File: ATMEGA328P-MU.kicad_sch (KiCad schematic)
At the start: 14 parts, among them J3 M20-9980345, U4 ATMEGA328P-MU, Y1 CSTNE16M0V530000R0

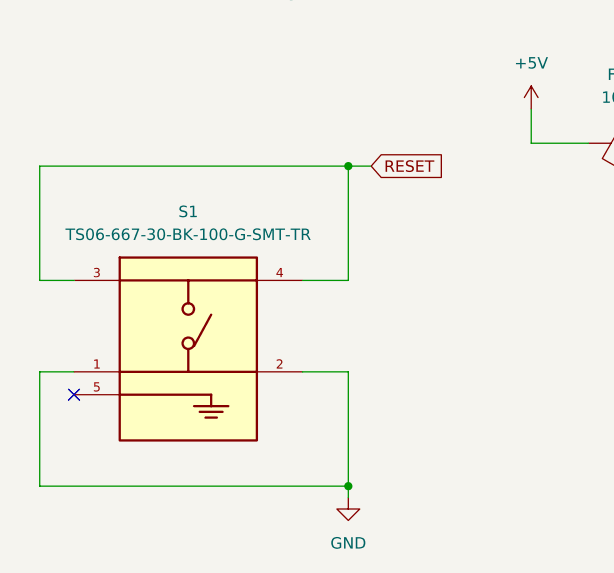
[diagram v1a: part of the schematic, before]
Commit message: Update Multiduino v2 design
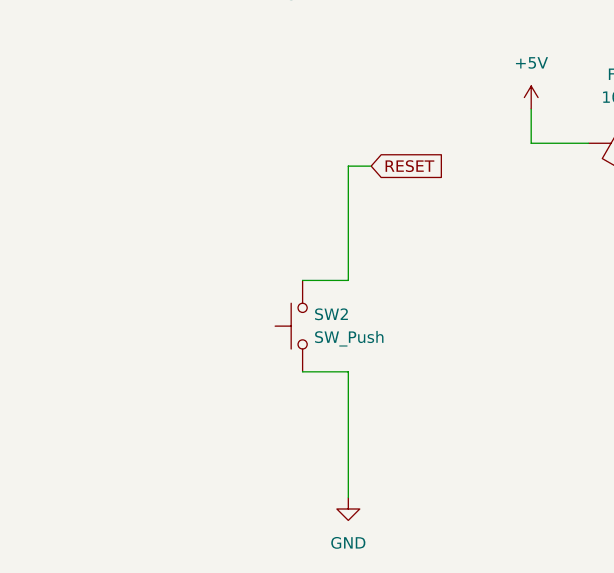
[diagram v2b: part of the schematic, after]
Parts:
- removed S1: TS06-667-30-BK-100-G-SMT-TR, Arduino Uno SMD:SW_TS06-667-30-BK-100-G-SMT-TR, symbol Arduino Uno SMD:TS06-667-30-BK-100-G-SMT-TR
- added SW2: SW_Push, Button_Switch_SMD:SW_Push_1P1T_NO_CK_KSC6xxJ, symbol Switch:SW_Push
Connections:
- net GND: now also SW2.1
- net RESET: now also SW2.2
- no-connect marks 3 -> 2
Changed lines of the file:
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@@
-	)
-	(junction
-		(at 78.74 142.24)
-		(diameter 0)
-		(color 0 0 0 0)
 	)
 	(junction
@@
 		(color 0 0 0 0)
 	)
-	(junction
-		(at 78.74 106.68)
-		(diameter 0)
-		(color 0 0 0 0)
-	)
 	(no_connect
 		(at 147.32 121.92)
 	)
 	(no_connect
-		(at 48.26 132.08)
-	)
-	(no_connect
 		(at 147.32 119.38)
 	)
 	(wire
 		(pts
-			(xy 78.74 142.24) (xy 44.45 142.24)
-		)
-		(stroke
-			(width 0)
-			(type default)
-		)
-	)
-	(wire
-		(pts
 			(xy 182.88 109.22) (xy 177.8 109.22)
 		)
@@
 	(wire
 		(pts
-			(xy 78.74 143.51) (xy 78.74 142.24)
+			(xy 78.74 129.54) (xy 78.74 143.51)
 		)
 		(stroke
@@
 	(wire
 		(pts
-			(xy 78.74 129.54) (xy 78.74 142.24)
-		)
-		(stroke
-			(width 0)
-			(type default)
-		)
-	)
-	(wire
-		(pts
 			(xy 135.89 106.68) (xy 135.89 107.95)
 		)
@@
 	(wire
 		(pts
-			(xy 44.45 142.24) (xy 44.45 129.54)
-		)
-		(stroke
-			(width 0)
-			(type default)
-		)
-	)
-	(wire
-		(pts
 			(xy 147.32 109.22) (xy 143.51 109.22)
 		)
@@
 	(wire
 		(pts
-			(xy 44.45 119.38) (xy 48.26 119.38)
-		)
-		(stroke
-			(width 0)
-			(type default)
-		)
-	)
-	(wire
-		(pts
 			(xy 144.78 95.25) (xy 144.78 101.6)
 		)
@@
 	(wire
 		(pts
-			(xy 44.45 106.68) (xy 44.45 119.38)
-		)
-		(stroke
-			(width 0)
-			(type default)
-		)
-	)
-	(wire
-		(pts
 			(xy 177.8 92.71) (xy 182.88 92.71)
-		)
-		(stroke
-			(width 0)
-			(type default)
-		)
-	)
-	(wire
-		(pts
-			(xy 44.45 106.68) (xy 78.74 106.68)
-		)
-		(stroke
-			(width 0)
-			(type default)
-		)
-	)
-	(wire
-		(pts
-			(xy 44.45 129.54) (xy 48.26 129.54)
 		)
 		(stroke
@@
 	)
 	(symbol
+		(lib_id "Switch:SW_Push")
+		(at 73.66 124.46 90)
+		(unit 1)
+		(exclude_from_sim no)
+		(in_bom yes)
+		(on_board yes)
+		(dnp no)
+		(fields_autoplaced yes)
+		(property "Reference" "SW2"
+			(at 74.93 123.1899 90)
+			(effects
+				(font
+					(size 1.27 1.27)
+				)
+				(justify right)
+			)
+		)
+		(property "Value" "SW_Push"
+			(at 74.93 125.7299 90)
+			(effects
+				(font
+					(size 1.27 1.27)
+				)
+				(justify right)
+			)
+		)
+		(property "Footprint" "Button_Switch_SMD:SW_Push_1P1T_NO_CK_KSC6xxJ"
+			(at 68.58 124.46 0)
+			(effects
+				(font
+					(size 1.27 1.27)
+				)
+				(hide yes)
+			)
+		)
+		(property "Datasheet" "~"
+			(at 68.58 124.46 0)
+			(effects
+				(font
+					(size 1.27 1.27)
+				)
+				(hide yes)
+			)
+		)
+		(property "Description" "Push button switch, generic, two pins"
+			(at 73.66 124.46 0)
+			(effects
+				(font
+					(size 1.27 1.27)
+				)
+				(hide yes)
+			)
+		)
+		(pin "2"
+		)
+		(pin "1"
+		)
+		(instances
+			(project "Multi-Duino"
+				(path "/a569fb01-6252-4b3a-9dcb-3675b5ce6f3f/2d22e81c-5a17-48ca-8b8a-97f7d3a7b1e3"
+					(reference "SW2")
+					(unit 1)
+				)
+			)
+		)
+	)
+	(symbol
 		(lib_id "Connector_Generic:Conn_02x03_Odd_Even")
 		(at 231.14 93.98 0)
@@
 					(unit 1)
 				)
-			)
-		)
-	)
-	(symbol
-		(lib_id "Arduino Uno SMD:TS06-667-30-BK-100-G-SMT-TR")
-		(at 60.96 127 0)
-		(unit 1)
-		(exclude_from_sim no)
-		(in_bom yes)
-		(on_board yes)
-		(dnp no)
-		(fields_autoplaced yes)
-		(property "Reference" "S1"
-			(at 60.96 111.76 0)
-			(effects
-				(font
-					(size 1.27 1.27)
-				)
-			)
-		)
-		(property "Value" "TS06-667-30-BK-100-G-SMT-TR"
-			(at 60.96 114.3 0)
-			(effects
-				(font
-					(size 1.27 1.27)
-				)
-			)
-		)
-		(property "Footprint" "Arduino Uno SMD:SW_TS06-667-30-BK-100-G-SMT-TR"
-			(at 61.722 142.24 0)
-			(effects
-				(font
-					(size 1.27 1.27)
-				)
-				(justify bottom)
-				(hide yes)
-			)
-		)
-		(property "Datasheet" ""
-			(at 60.96 127 0)
-			(effects
-				(font
-					(size 1.27 1.27)
-				)
-				(hide yes)
-			)
-		)
-		(property "Description" ""
-			(at 60.96 127 0)
-			(effects
-				(font
-					(size 1.27 1.27)
-				)
-				(hide yes)
-			)
-		)
-		(property "PARTREV" "1.0"
-			(at 60.96 113.792 0)
-			(effects
-				(font
-					(size 1.27 1.27)
-				)
-				(justify bottom)
-				(hide yes)
-			)
-		)
-		(property "MANUFACTURER" "Cui Devices"
-			(at 61.722 111.76 0)
-			(effects
-				(font
-					(size 1.27 1.27)
-				)
-				(justify bottom)
-				(hide yes)
-			)
-		)
-		(property "MAXIMUM_PACKAGE_HEIGHT" "2.6 mm"
-			(at 61.468 109.728 0)
-			(effects
-				(font
-					(size 1.27 1.27)
-				)
-				(justify bottom)
-				(hide yes)
-			)
-		)
-		(property "STANDARD" "Manufacturer Recommendations"
-			(at 62.484 107.696 0)
-			(effects
-				(font
-					(size 1.27 1.27)
-				)
-				(justify bottom)
-				(hide yes)
-			)
-		)
-		(pin "5"
-		)
-		(pin "4"
-		)
-		(pin "3"
-		)
-		(pin "1"
-		)
-		(pin "2"
-		)
-		(instances
-			(project "Multi-Duino"
-				(path "/a569fb01-6252-4b3a-9dcb-3675b5ce6f3f/2d22e81c-5a17-48ca-8b8a-97f7d3a7b1e3"
-					(reference "S1")
-					(unit 1)
-				)
